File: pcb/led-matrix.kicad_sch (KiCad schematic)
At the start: 64 parts

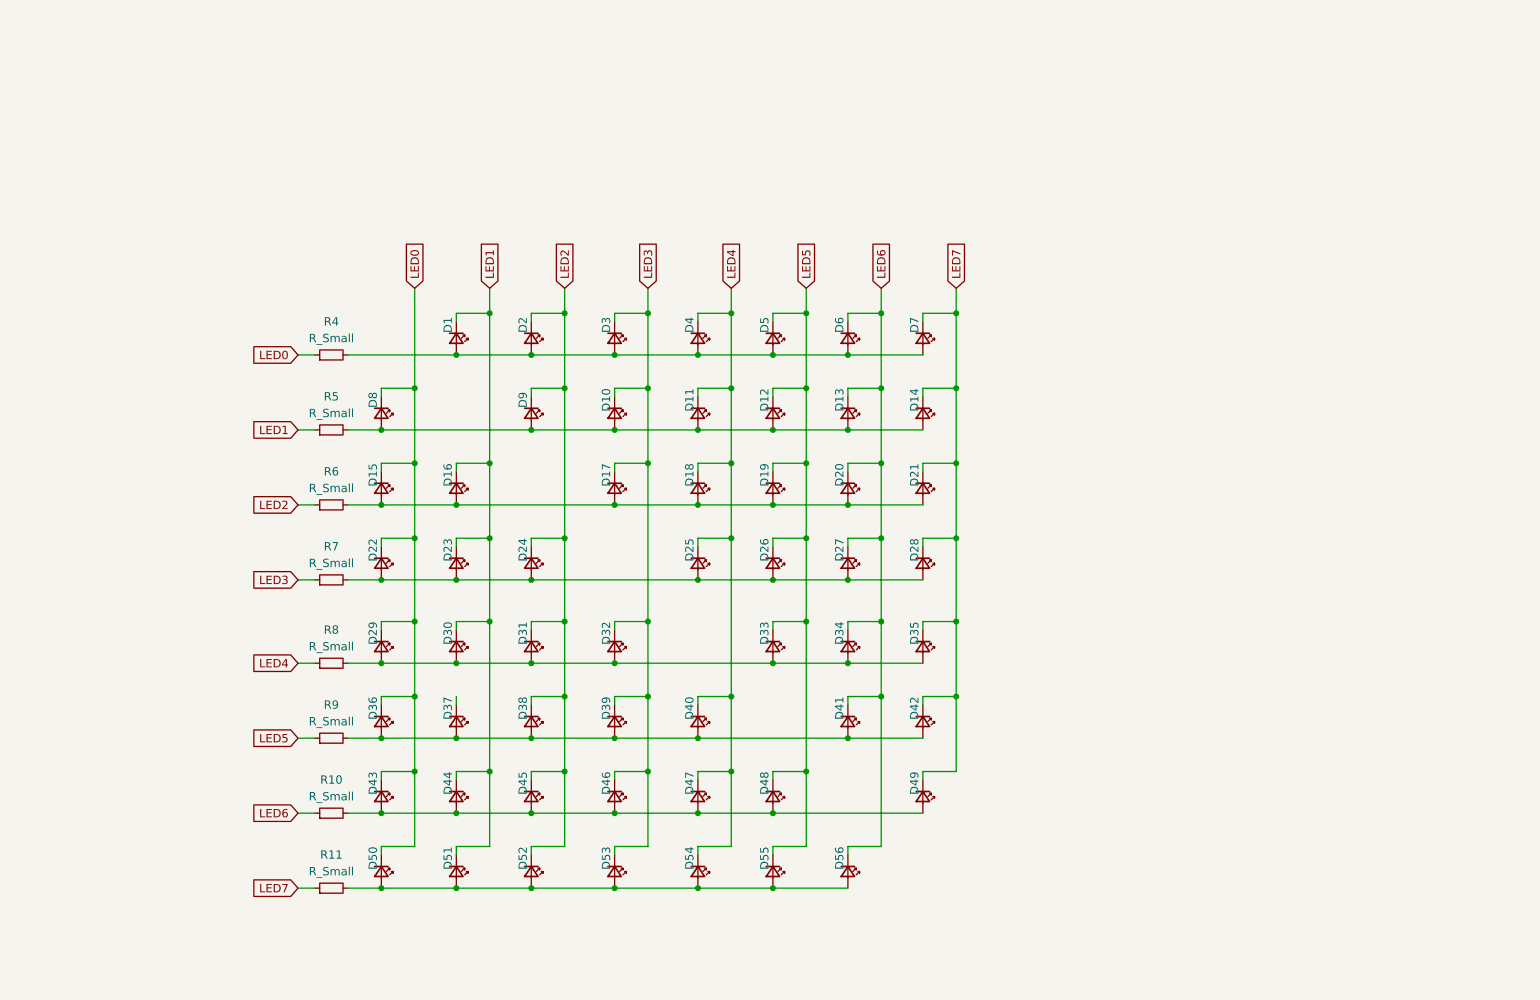
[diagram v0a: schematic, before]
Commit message: Added footprints, except for the USB port
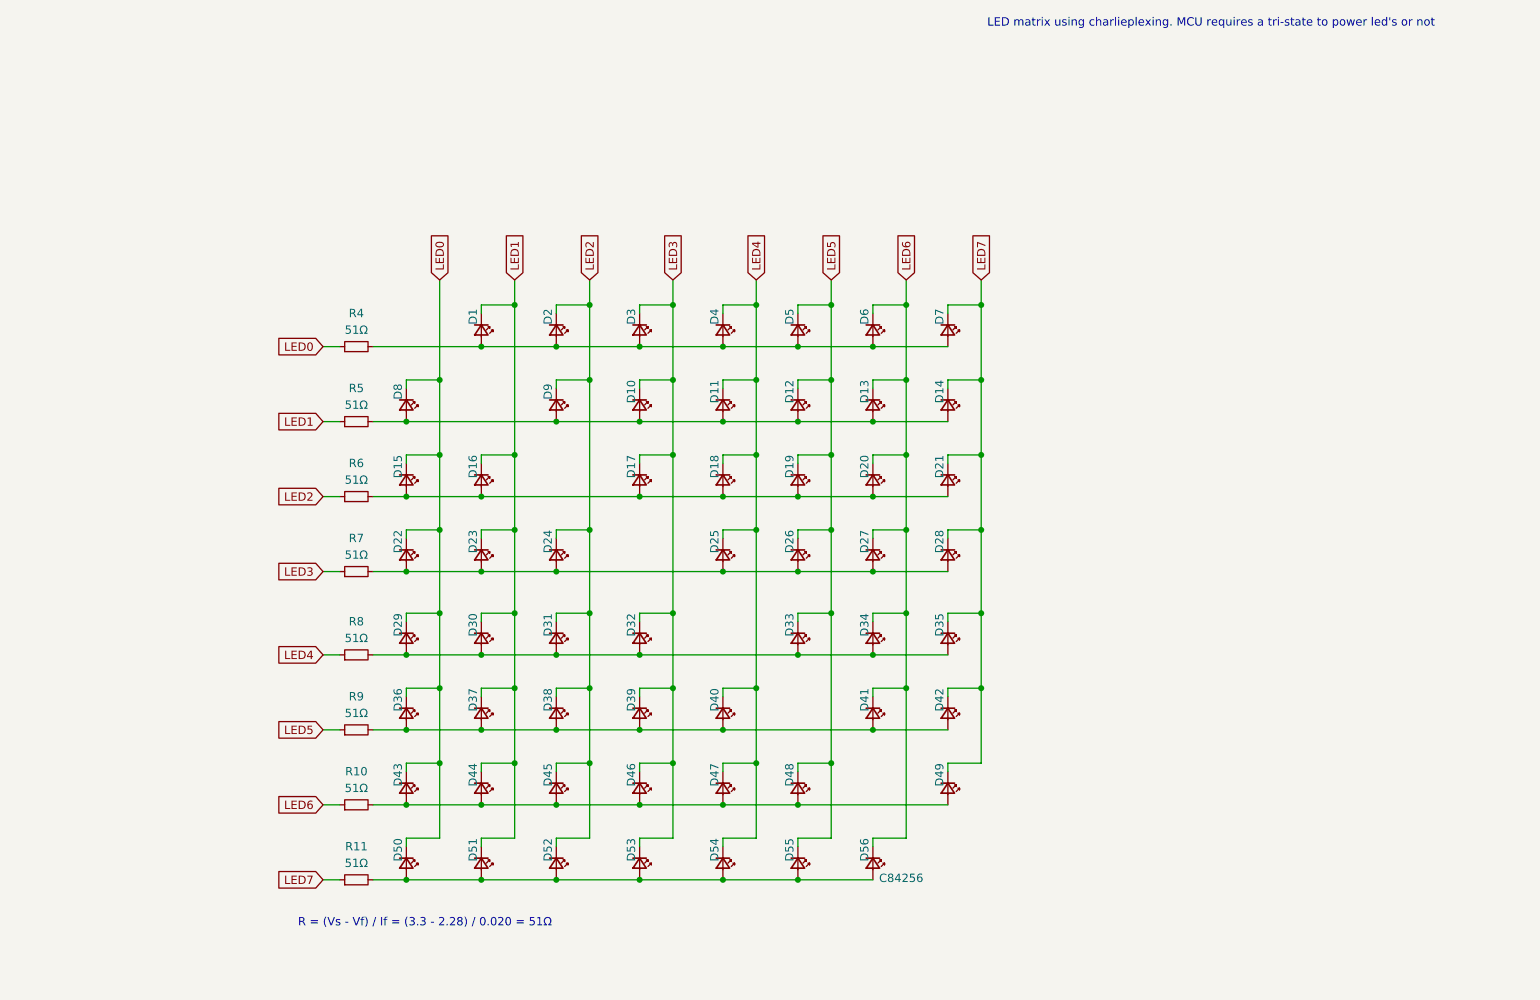
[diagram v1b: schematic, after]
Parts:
- D1, D10, D11, D12, D13, D14, D15, D16, D17, D18, D19, D2, D20, D21, D22, D23, D24, D25, D26, D27, D28, D29, D3, D30, D31, D32, D33, D34, D35, D36, D37, D38, D39, D4, D40, D41, D42, D43, D44, D45, D46, D47, D48, D49, D5, D50, D51, D52, D53, D54, D55, D56, D6, D7, D8, D9: footprint (none) -> LED_SMD:LED_0805_2012Metric; lcsc (none) -> C84256
- R10, R11, R4, R5, R6, R7, R8, R9: value R_Small -> 51Ω; footprint (none) -> Resistor_SMD:R_0603_1608Metric; lcsc (none) -> C23197
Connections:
- net LED1: now also D37.1 (K)
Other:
- note added: "LED matrix using charlieplexing. MCU requires a tri-state to power led's or not"
- note added: "R = (Vs - Vf) / If = (3.3 - 2.28) / 0.020 = 51Ω"
- moved on the sheet: D1, D10, D11, D12, D13, D14, D15, D16, D17, D18, D19, D2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

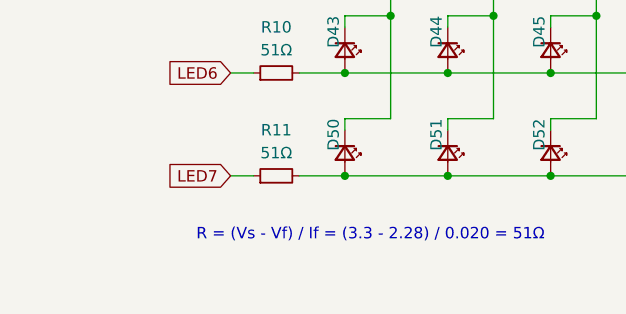
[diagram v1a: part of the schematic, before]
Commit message: Added footprint for usb port
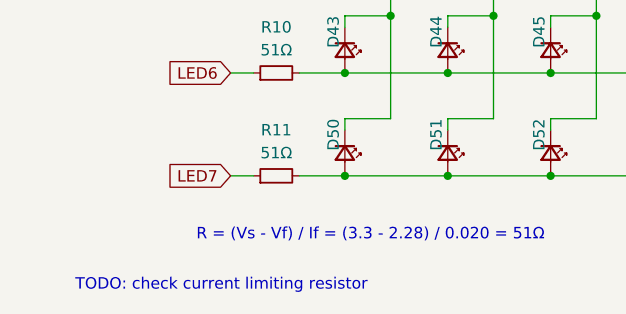
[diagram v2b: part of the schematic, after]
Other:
- note added: "TODO: check current limiting resistor"
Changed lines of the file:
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@@
+		)
+	)
+	(text "TODO: check current limiting resistor"
+		(exclude_from_sim no)
+		(at 105.664 159.512 0)
+		(effects
+			(font
+				(size 1.27 1.27)
+			)
 		)
 	)

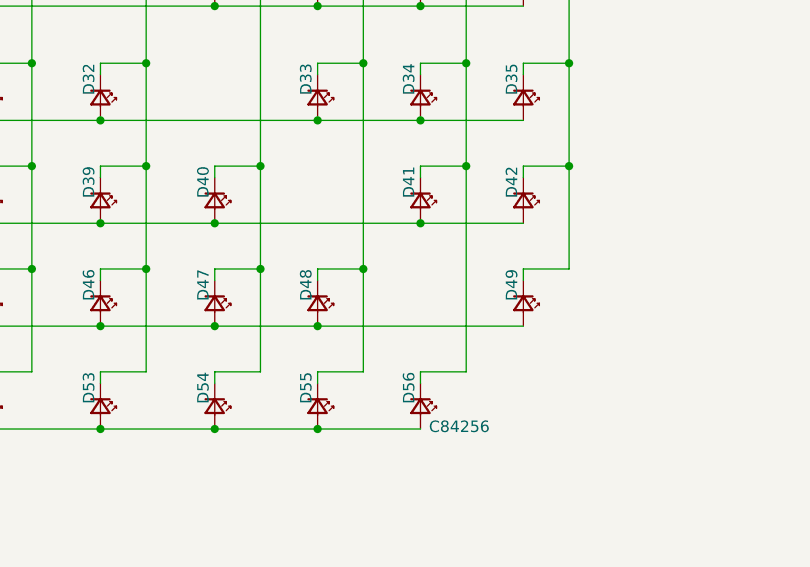
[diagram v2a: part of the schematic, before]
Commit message: Started working on PCB layout
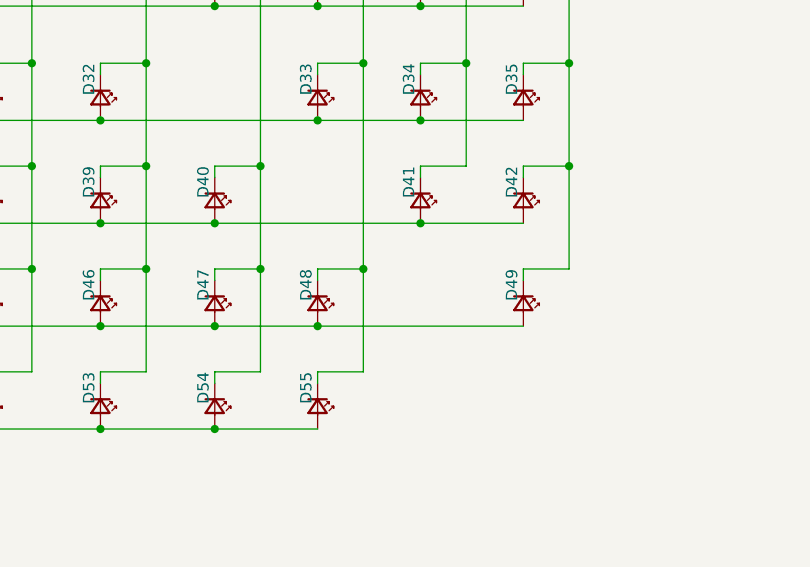
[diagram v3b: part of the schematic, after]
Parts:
- removed D56: LED_Small, LED_SMD:LED_0805_2012Metric, symbol Device:LED_Small
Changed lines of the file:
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@@
 	)
 	(junction
-		(at 195.58 118.11)
-		(diameter 0)
-		(color 0 0 0 0)
-	)
-	(junction
-		(at 179.07 147.32)
-		(diameter 0)
-		(color 0 0 0 0)
-	)
-	(junction
 		(at 179.07 88.9)
 		(diameter 0)
@@
 	(wire
 		(pts
-			(xy 190.5 142.24) (xy 190.5 140.97)
-		)
-		(stroke
-			(width 0)
-			(type default)
-		)
-	)
-	(wire
-		(pts
 			(xy 201.93 83.82) (xy 201.93 82.55)
 		)
@@
 	(wire
 		(pts
-			(xy 195.58 118.11) (xy 195.58 140.97)
-		)
-		(stroke
-			(width 0)
-			(type default)
-		)
-	)
-	(wire
-		(pts
 			(xy 135.89 106.68) (xy 135.89 118.11)
 		)
@@
 	(wire
 		(pts
-			(xy 190.5 140.97) (xy 195.58 140.97)
-		)
-		(stroke
-			(width 0)
-			(type default)
-		)
-	)
-	(wire
-		(pts
 			(xy 190.5 71.12) (xy 195.58 71.12)
 		)
@@
 	(wire
 		(pts
-			(xy 179.07 147.32) (xy 190.5 147.32)
-		)
-		(stroke
-			(width 0)
-			(type default)
-		)
-	)
-	(wire
-		(pts
 			(xy 179.07 95.25) (xy 179.07 93.98)
 		)
@@
 					(unit 1)
 				)
-			)
-		)
-	)
-	(symbol
-		(lib_id "Device:LED_Small")
-		(at 190.5 144.78 270)
-		(unit 1)
-		(exclude_from_sim no)
-		(in_bom yes)
-		(on_board yes)
-		(dnp no)
-		(property "Reference" "D56"
-			(at 189.23 142.748 0)
-			(effects
-				(font
-					(size 1.27 1.27)
-				)
-			)
-		)
-		(property "Value" "LED_Small"
-			(at 186.69 144.8435 0)
-			(effects
-				(font
-					(size 1.27 1.27)
-				)
-				(hide yes)
-			)
-		)
-		(property "Footprint" "LED_SMD:LED_0805_2012Metric"
-			(at 190.5 144.78 90)
-			(effects
-				(font
-					(size 1.27 1.27)
-				)
-				(hide yes)
-			)
-		)
-		(property "Datasheet" "https://wmsc.lcsc.com/wmsc/upload/file/pdf/v2/lcsc/2304140030_Foshan-NationStar-Optoelectronics-NCD0805R1_C84256.pdf"
-			(at 190.5 144.78 90)
-			(effects
-				(font
-					(size 1.27 1.27)
-				)
-				(hide yes)
-			)
-		)
-		(property "Description" "Light emitting diode, small symbol"
-			(at 190.5 144.78 0)
-			(effects
-				(font
-					(size 1.27 1.27)
-				)
-				(hide yes)
-			)
-		)
-		(property "lcsc" "C84256"
-			(at 194.818 147.066 90)
-			(effects
-				(font
-					(size 1.27 1.27)
-				)
-			)
-		)
-		(pin "1"
-		)
-		(pin "2"
-		)
-		(instances
-			(project "virm-stm32"
-				(path "/8ee1ec31-71f0-4848-90a2-86703fa56028/43e012f4-5a94-4351-9f48-2b43d14e4308"
-					(reference "D56")
-					(unit 1)
-				)

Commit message: started routing, with additional leds
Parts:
- added D17, D18, D26, D27, D35, D36, D44, D45, D53, D54, D62, D63, D70, D71, D72, D73, D74, D75, D76, D77, D78, D79, D8, D80, D81, D82, D83, D84, D85, D86, D87, D88, D89, D9, D90: LED_Small, LED_SMD:LED_0805_2012Metric, symbol Device:LED_Small
- added R12, R13: 51Ω, Resistor_SMD:R_0603_1608Metric, symbol Device:R_Small
- renumbered D8 to D10, D9 to D11, D10 to D12, D11 to D13, D12 to D14, D13 to D15, D14 to D16, D15 to D19, D16 to D20, D17 to D21, D18 to D22, D19 to D23, D20 to D24, D21 to D25, D22 to D28, D23 to D29, D24 to D30, D25 to D31, D26 to D32, D27 to D33, D28 to D34, D29 to D37, D30 to D38, D31 to D39, D32 to D40, D33 to D41, D34 to D42, D35 to D43, D36 to D46, D37 to D47, D38 to D48, D39 to D49, D40 to D50, D41 to D51, D42 to D52, D43 to D55, D44 to D56, D45 to D57, D46 to D58, D47 to D59, D48 to D60, D49 to D61, D50 to D64, D51 to D65, D52 to D66, D53 to D67, D54 to D68, D55 to D69
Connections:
- net LED0: now also D73.1 (K), D82.1 (K)
- net LED1: now also D74.1 (K), D83.1 (K)
- net LED2: now also D75.1 (K), D84.1 (K)
- net LED3: now also D76.1 (K), D85.1 (K)
- net LED4: now also D77.1 (K), D86.1 (K)
- net LED5: now also D78.1 (K), D87.1 (K)
- net LED6: now also D70.1 (K), D79.1 (K), D88.1 (K)
- net LED7: now also D80.1 (K), D89.1 (K)
- net at D46.2 (A), D47.2 (A), D48.2 (A)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: now also D53.2 (A), D54.2 (A)
- net at D55.2 (A), D56.2 (A), D57.2 (A)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: now also D62.2 (A), D63.2 (A)
- net at D64.2 (A), D65.2 (A), D66.2 (A)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: now also D70.2 (A), D71.2 (A), D72.2 (A)
- net at D19.2 (A), D20.2 (A), D21.2 (A)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: now also D26.2 (A), D27.2 (A)
- net at D37.2 (A), D38.2 (A), D39.2 (A)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: now also D44.2 (A), D45.2 (A)
- net at D10.2 (A), D11.2 (A), D12.2 (A)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: now also D17.2 (A), D18.2 (A)
- net at D1.2 (A), D2.2 (A), D3.2 (A)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: now also D8.2 (A), D9.2 (A)
- net at D28.2 (A), D29.2 (A), D30.2 (A)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: now also D35.2 (A), D36.2 (A)
- new net: D73.2 (A), D74.2 (A), D75.2 (A), D76.2 (A), D77.2 (A), D78.2 (A), D79.2 (A), D80.2 (A), D81.2 (A), R12.2
- new net: D82.2 (A), D83.2 (A), D84.2 (A), D85.2 (A), D86.2 (A), D87.2 (A), D88.2 (A), D89.2 (A), D90.2 (A), R13.2
- new net LED8: D17.1 (K), D26.1 (K), D35.1 (K), D44.1 (K), D53.1 (K), D62.1 (K), D71.1 (K), D8.1 (K), D90.1 (K), R12.1
- new net LED9: D18.1 (K), D27.1 (K), D36.1 (K), D45.1 (K), D54.1 (K), D63.1 (K), D72.1 (K), D81.1 (K), D9.1 (K), R13.1
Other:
- moved on the sheet: D1, D10, D11, D12, D13, D14, D15, D16, D19, D2, D20, D21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
